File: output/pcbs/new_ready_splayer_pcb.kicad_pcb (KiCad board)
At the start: 2 copper layers, 124.4 x 92.7 mm, 36 parts

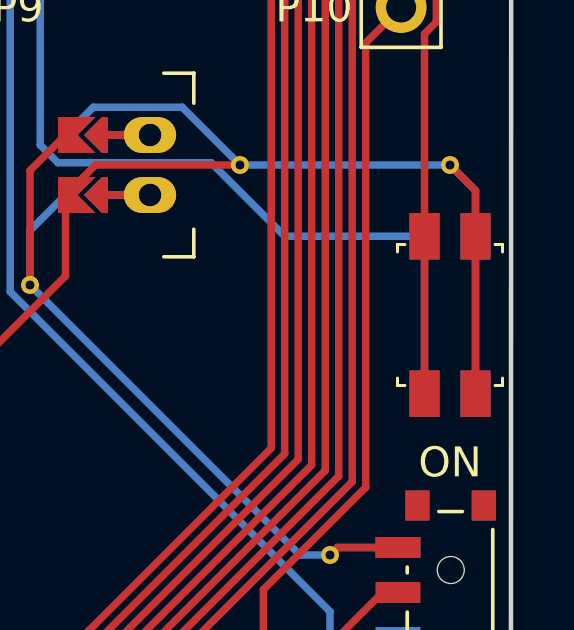
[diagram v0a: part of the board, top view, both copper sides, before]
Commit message: drilled holes for reset side buttons
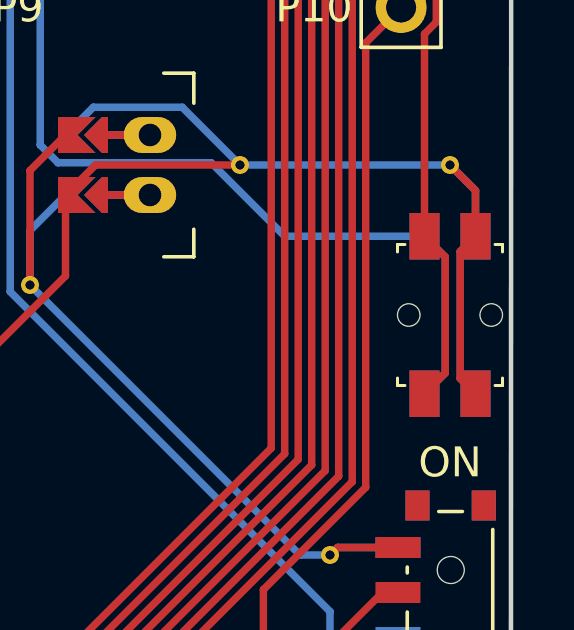
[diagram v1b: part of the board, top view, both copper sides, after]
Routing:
- net RST: track 115.9 -> 117.1 mm
- net GND: track 874.0 -> 874.9 mm
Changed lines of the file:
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@@
 			(layer "Dwgs.User")
 		)
+		(pad "" np_thru_hole circle
+			(at 0 -1.375 90)
+			(size 0.75 0.75)
+			(drill 0.75)
+			(layers "F&B.Cu" "*.Mask")
+		)
+		(pad "" np_thru_hole circle
+			(at 0 1.375 90)
+			(size 0.75 0.75)
+			(drill 0.75)
+			(layers "F&B.Cu" "*.Mask")
+		)
 		(pad "1" smd rect
 			(at -2.625 -0.85 90)
@@
 	)
 	(segment
-		(start 272.009009 131.280853)
-		(end 272.009009 136.530853)
-		(width 0.25)
-		(layer "F.Cu")
-		(net 2)
-	)
-	(segment
 		(start 155.486085 122.220706)
 		(end 159.280028 124.877254)
@@
 	)
 	(segment
+		(start 271.5 136.021844)
+		(end 272.009009 136.530853)
+		(width 0.25)
+		(layer "F.Cu")
+		(net 2)
+	)
+	(segment
 		(start 152.534062 105.478973)
 		(end 156.328007 108.13552)
@@
 	)
 	(segment
+		(start 272.009009 131.280853)
+		(end 271.5 131.789862)
+		(width 0.25)
+		(layer "F.Cu")
+		(net 2)
+	)
+	(segment
 		(start 251.242892 139.705853)
 		(end 258.343007 132.605738)
@@
 	)
 	(segment
+		(start 271.5 131.789862)
+		(end 271.5 136.021844)
+		(width 0.25)
+		(layer "F.Cu")
+		(net 2)
+	)
+	(segment
 		(start 272.009009 131.280853)
 		(end 272.009009 129.755851)
@@
 	)
 	(segment
-		(start 272.009009 131.280853)
-		(end 272.009009 136.530853)
-		(width 0.25)
-		(layer "B.Cu")
-		(net 2)
-	)
-	(segment
 		(start 187.655837 138.748078)
 		(end 190.974651 135.189085)
@@
 	)
 	(segment
+		(start 271.5 131.789862)
+		(end 271.5 136.021844)
+		(width 0.25)
+		(layer "B.Cu")
+		(net 2)
+	)
+	(segment
 		(start 173.994325 131.878507)
 		(end 174.73667 136.08856)
@@
 	)
 	(segment
+		(start 271.5 136.021844)
+		(end 272.009009 136.530853)
+		(width 0.25)
+		(layer "B.Cu")
+		(net 2)
+	)
+	(segment
 		(start 230.934009 127.155852)
 		(end 231.209014 127.155852)
@@
 	)
 	(segment
+		(start 272.009009 131.280853)
+		(end 271.5 131.789862)
+		(width 0.25)
+		(layer "B.Cu")
+		(net 2)
+	)
+	(segment
 		(start 231.209014 127.155852)
 		(end 235.659011 122.705855)
@@
 	)
 	(segment
-		(start 270.309009 136.530853)
+		(start 270.015701 101.97)
+		(end 259.684 101.97)
+		(width 0.25)
+		(layer "F.Cu")
+		(net 21)
+	)
+	(segment
+		(start 271 131.971844)
 		(end 270.309009 131.280853)
 		(width 0.25)
@@
 	)
 	(segment
-		(start 270.015701 101.97)
-		(end 259.684 101.97)
+		(start 270.309009 136.530853)
+		(end 271 135.839862)
 		(width 0.25)
 		(layer "F.Cu")
@@
 	)
 	(segment
+		(start 271 135.839862)
+		(end 271 131.971844)
+		(width 0.25)
+		(layer "F.Cu")
+		(net 21)
+	)
+	(segment
 		(start 270.015701 99.62)
 		(end 267.229 99.62)
@@
 	)
 	(segment
+		(start 271 135.839862)
+		(end 270.309009 136.530853)
+		(width 0.25)
+		(layer "B.Cu")
+		(net 21)
+	)
+	(segment
 		(start 266.684 100.165)
 		(end 266.684 100.795)
@@
 	)
 	(segment
+		(start 270.309009 131.280853)
+		(end 271 131.971844)
+		(width 0.25)
+		(layer "B.Cu")
+		(net 21)
+	)
+	(segment
 		(start 266.334313 100.794852)
 		(end 265.609317 100.069851)
@@
 	)
 	(segment
+		(start 271 131.971844)
+		(end 271 135.839862)
+		(width 0.25)
+		(layer "B.Cu")
+		(net 21)
+	)
+	(segment
 		(start 267.99 104.51)
 		(end 270.015701 104.51)
@@
 		(width 0.25)
 		(layer "B.Cu")
-		(net 21)
-	)
-	(segment
-		(start 270.309009 131.280853)
-		(end 270.309009 136.530853)
-		(width 0.25)
-		(layer "B.Cu")
